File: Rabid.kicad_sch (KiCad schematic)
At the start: 222 parts, among them J1 USB Header, SW1 Esc, SW10 A, SW100 Unused, SW101 Unused, SW102 →, SW11 Z, SW12 LMeta, SW13 F1, SW14 2, SW15 W, SW16 S, SW17 X, SW18 LAlt, SW19 F2, SW20 3, SW21 E, SW22 D, SW23 C, SW24 Unused, SW25 F3, SW26 4, SW27 R, SW28 F, SW29 V, SW3 Tab, SW30 Unused, SW31 F4, SW32 5, SW33 T, SW34 G, SW35 B, SW36 Unused, SW37 F5, SW38 6, SW39 Y, SW4 CapsLk, SW40 H, SW41 N, SW42 Space, SW43 F6, SW44 7, SW45 U, SW46 J, SW47 M, SW48 Unused, SW49 F7, SW5 LShift, SW50 8, SW51 I, SW52 K, SW53 ,, SW54 Unused, SW55 F8, SW56 9, SW57 O, SW58 L, SW59 ., SW6 LCtrl, SW60 Unused, SW61 F9, SW62 0, SW63 P, SW64 ;, SW65 /, SW66 AltGr, SW67 F10, SW68 -, SW69 [, SW7 Unused, SW70 ", SW71 RShift, SW72 RMeta, SW73 F11, SW74 =, SW75 ], SW76 ↲, SW77 Unused, SW78 Fn, SW79 F12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

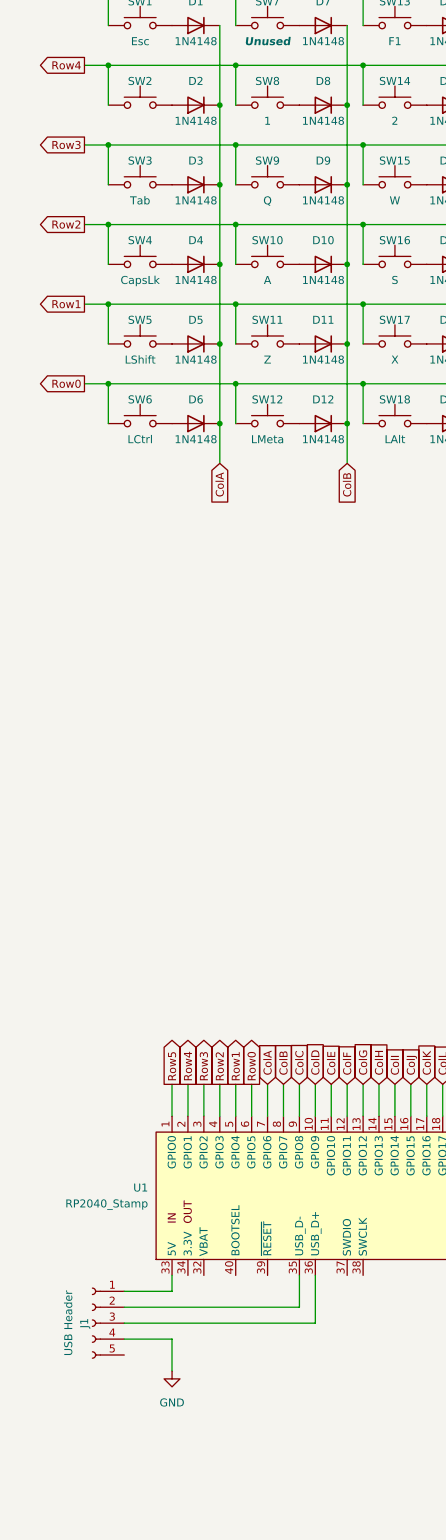
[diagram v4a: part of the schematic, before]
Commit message: Tidy up the USB connector nets.
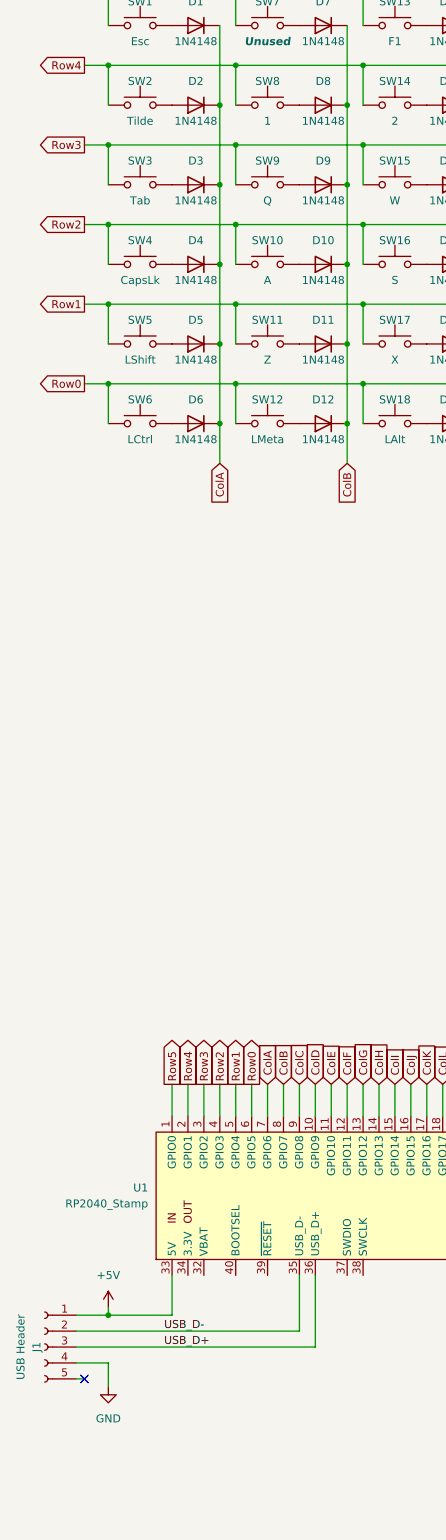
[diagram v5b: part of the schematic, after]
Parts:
- SW2: value ~ -> Tilde
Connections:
- net +5V: now reaches J1.1 (Pin_1), U1.33 (5V)
- net USB_D-: now reaches J1.2 (Pin_2), U1.35 (USB_D-)
- net USB_D+: now reaches J1.3 (Pin_3), U1.36 (USB_D+)
- no-connect marks 0 -> 1
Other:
- moved on the sheet: J1
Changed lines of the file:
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@@
   (junction (at 246.38 60.96) (diameter 0) (color 0 0 0 0)
   )
+  (junction (at 43.18 234.95) (diameter 0) (color 0 0 0 0)
+  )
   (junction (at 167.64 200.66) (diameter 0) (color 0 0 0 0)
   )
@@
   (junction (at 226.06 60.96) (diameter 0) (color 0 0 0 0)
   )
+  (no_connect (at 39.37 245.11))
   (wire (pts (xy 185.42 35.56) (xy 185.42 41.91))
     (stroke (width 0) (type default) (color 0 0 0 0))
@@
     (stroke (width 0) (type default) (color 0 0 0 0))
   )
-  (wire (pts (xy 45.72 236.22) (xy 76.2 236.22))
+  (wire (pts (xy 148.59 204.47) (xy 148.59 200.66))
     (stroke (width 0) (type default) (color 0 0 0 0))
   )
-  (wire (pts (xy 148.59 204.47) (xy 148.59 200.66))
+  (wire (pts (xy 38.1 240.03) (xy 76.2 240.03))
     (stroke (width 0) (type default) (color 0 0 0 0))
   )
@@
     (stroke (width 0) (type default) (color 0 0 0 0))
   )
+  (wire (pts (xy 38.1 242.57) (xy 43.18 242.57))
+    (stroke (width 0) (type default) (color 0 0 0 0))
+  )
   (wire (pts (xy 153.67 191.77) (xy 148.59 191.77))
     (stroke (width 0) (type default) (color 0 0 0 0))
@@
     (stroke (width 0) (type default) (color 0 0 0 0))
   )
-  (wire (pts (xy 45.72 238.76) (xy 53.34 238.76))
-    (stroke (width 0) (type default) (color 0 0 0 0))
-  )
   (wire (pts (xy 347.98 86.36) (xy 368.3 86.36))
     (stroke (width 0) (type default) (color 0 0 0 0))
@@
     (stroke (width 0) (type default) (color 0 0 0 0))
   )
+  (wire (pts (xy 43.18 233.68) (xy 43.18 234.95))
+    (stroke (width 0) (type default) (color 0 0 0 0))
+  )
   (wire (pts (xy 327.66 60.96) (xy 347.98 60.96))
     (stroke (width 0) (type default) (color 0 0 0 0))
@@
     (stroke (width 0) (type default) (color 0 0 0 0))
   )
-  (wire (pts (xy 53.34 228.6) (xy 53.34 231.14))
-    (stroke (width 0) (type default) (color 0 0 0 0))
-  )
   (wire (pts (xy 264.16 29.21) (xy 264.16 41.91))
     (stroke (width 0) (type default) (color 0 0 0 0))
@@
     (stroke (width 0) (type default) (color 0 0 0 0))
   )
+  (wire (pts (xy 38.1 234.95) (xy 43.18 234.95))
+    (stroke (width 0) (type default) (color 0 0 0 0))
+  )
   (wire (pts (xy 78.74 198.12) (xy 78.74 203.2))
     (stroke (width 0) (type default) (color 0 0 0 0))
@@
     (stroke (width 0) (type default) (color 0 0 0 0))
   )
-  (wire (pts (xy 45.72 233.68) (xy 73.66 233.68))
-    (stroke (width 0) (type default) (color 0 0 0 0))
-  )
   (wire (pts (xy 144.78 35.56) (xy 165.1 35.56))
     (stroke (width 0) (type default) (color 0 0 0 0))
@@
     (stroke (width 0) (type default) (color 0 0 0 0))
   )
+  (wire (pts (xy 38.1 245.11) (xy 39.37 245.11))
+    (stroke (width 0) (type default) (color 0 0 0 0))
+  )
   (wire (pts (xy 165.1 73.66) (xy 165.1 80.01))
     (stroke (width 0) (type default) (color 0 0 0 0))
@@
     (stroke (width 0) (type default) (color 0 0 0 0))
   )
+  (wire (pts (xy 43.18 234.95) (xy 53.34 234.95))
+    (stroke (width 0) (type default) (color 0 0 0 0))
+  )
   (wire (pts (xy 182.88 67.31) (xy 182.88 80.01))
     (stroke (width 0) (type default) (color 0 0 0 0))
@@
     (stroke (width 0) (type default) (color 0 0 0 0))
   )
-  (wire (pts (xy 76.2 236.22) (xy 76.2 228.6))
-    (stroke (width 0) (type default) (color 0 0 0 0))
-  )
   (wire (pts (xy 347.98 48.26) (xy 368.3 48.26))
     (stroke (width 0) (type default) (color 0 0 0 0))
@@
     (stroke (width 0) (type default) (color 0 0 0 0))
   )
-  (wire (pts (xy 53.34 238.76) (xy 53.34 243.84))
-    (stroke (width 0) (type default) (color 0 0 0 0))
-  )
   (wire (pts (xy 165.1 86.36) (xy 165.1 92.71))
     (stroke (width 0) (type default) (color 0 0 0 0))
@@
     (stroke (width 0) (type default) (color 0 0 0 0))
   )
+  (wire (pts (xy 43.18 242.57) (xy 43.18 246.38))
+    (stroke (width 0) (type default) (color 0 0 0 0))
+  )
   (wire (pts (xy 161.29 224.79) (xy 167.64 224.79))
     (stroke (width 0) (type default) (color 0 0 0 0))
@@
     (stroke (width 0) (type default) (color 0 0 0 0))
   )
+  (wire (pts (xy 73.66 237.49) (xy 73.66 228.6))
+    (stroke (width 0) (type default) (color 0 0 0 0))
+  )
   (wire (pts (xy 185.42 48.26) (xy 205.74 48.26))
     (stroke (width 0) (type default) (color 0 0 0 0))
@@
     (stroke (width 0) (type default) (color 0 0 0 0))
   )
-  (wire (pts (xy 162.56 41.91) (xy 162.56 54.61))
+  (wire (pts (xy 38.1 237.49) (xy 73.66 237.49))
     (stroke (width 0) (type default) (color 0 0 0 0))
   )
-  (wire (pts (xy 43.18 73.66) (xy 63.5 73.66))
+  (wire (pts (xy 162.56 41.91) (xy 162.56 54.61))
     (stroke (width 0) (type default) (color 0 0 0 0))
   )
-  (wire (pts (xy 73.66 233.68) (xy 73.66 228.6))
+  (wire (pts (xy 43.18 73.66) (xy 63.5 73.66))
     (stroke (width 0) (type default) (color 0 0 0 0))
   )
@@
     (stroke (width 0) (type default) (color 0 0 0 0))
   )
-  (wire (pts (xy 53.34 231.14) (xy 45.72 231.14))
-    (stroke (width 0) (type default) (color 0 0 0 0))
-  )
   (wire (pts (xy 43.18 22.86) (xy 63.5 22.86))
     (stroke (width 0) (type default) (color 0 0 0 0))
@@
     (stroke (width 0) (type default) (color 0 0 0 0))
   )
+  (wire (pts (xy 76.2 240.03) (xy 76.2 228.6))
+    (stroke (width 0) (type default) (color 0 0 0 0))
+  )
   (wire (pts (xy 83.82 48.26) (xy 83.82 54.61))
     (stroke (width 0) (type default) (color 0 0 0 0))
@@
     (stroke (width 0) (type default) (color 0 0 0 0))
   )
+  (wire (pts (xy 53.34 234.95) (xy 53.34 228.6))
+    (stroke (width 0) (type default) (color 0 0 0 0))
+  )
   (wire (pts (xy 83.82 86.36) (xy 104.14 86.36))
     (stroke (width 0) (type default) (color 0 0 0 0))
@@
     (stroke (width 0) (type default) (color 0 0 0 0))
   )
+  (label "USB_D-" (at 52.07 237.49 0)
+    (effects (font (size 1.27 1.27)) (justify left bottom))
+  )
+  (label "USB_D+" (at 52.07 240.03 0)
+    (effects (font (size 1.27 1.27)) (justify left bottom))
+  )
   (global_label "ColE" (shape input) (at 78.74 198.12 90) (fields_autoplaced)
     (effects (font (size 1.27 1.27)) (justify left))
@@
     (pin "2")
   )
+  (symbol (lib_id "power:+5V") (at 43.18 233.68 0) (unit 1)
+    (in_bom yes) (on_board yes) (fields_autoplaced)
+    (property "Reference" "#PWR0101" (id 0) (at 43.18 237.49 0)
+      (effects (font (size 1.27 1.27)) hide)
+    )
+    (property "Value" "+5V" (id 1) (at 43.18 228.6 0))
+    (property "Footprint" "" (id 2) (at 43.18 233.68 0)
+      (effects (font (size 1.27 1.27)) hide)
+    )
+    (property "Datasheet" "" (id 3) (at 43.18 233.68 0)
+      (effects (font (size 1.27 1.27)) hide)
+    )
+    (pin "1")
+  )
   (symbol (lib_id "Switch:SW_Push") (at 48.26 54.61 0) (unit 1)
     (in_bom yes) (on_board yes)
@@
     (pin "2")
   )
-  (symbol (lib_id "power:GND") (at 53.34 243.84 0) (unit 1)
+  (symbol (lib_id "power:GND") (at 43.18 246.38 0) (unit 1)
     (in_bom yes) (on_board yes) (fields_autoplaced)
-    (property "Reference" "#PWR01" (id 0) (at 53.34 250.19 0)
+    (property "Reference" "#PWR01" (id 0) (at 43.18 252.73 0)
       (effects (font (size 1.27 1.27)) hide)
     )
-    (property "Value" "GND" (id 1) (at 53.34 248.92 0))
-    (property "Footprint" "" (id 2) (at 53.34 243.84 0)
+    (property "Value" "GND" (id 1) (at 43.18 251.46 0))
+    (property "Footprint" "" (id 2) (at 43.18 246.38 0)
       (effects (font (size 1.27 1.27)) hide)
     )
-    (property "Datasheet" "" (id 3) (at 53.34 243.84 0)
+    (property "Datasheet" "" (id 3) (at 43.18 246.38 0)
       (effects (font (size 1.27 1.27)) hide)
     )
@@
     (pin "2")
   )
-  (symbol (lib_id "Connector:Conn_01x05_Female") (at 40.64 236.22 0) (mirror y) (unit 1)
+  (symbol (lib_id "Connector:Conn_01x05_Female") (at 33.02 240.03 0) (mirror y) (unit 1)
     (in_bom yes) (on_board yes)
-    (property "Reference" "J1" (id 0) (at 39.37 236.22 90))
-    (property "Value" "USB Header" (id 1) (at 36.83 236.22 90))
-    (property "Footprint" "Connector_JST:JST_PH_S5B-PH-SM4-TB_1x05-1MP_P2.00mm_Horizontal" (id 2) (at 40.64 236.22 0)
+    (property "Reference" "J1" (id 0) (at 31.75 240.03 90))
+    (property "Value" "USB Header" (id 1) (at 29.21 240.03 90))
+    (property "Footprint" "Connector_JST:JST_PH_S5B-PH-SM4-TB_1x05-1MP_P2.00mm_Horizontal" (id 2) (at 33.02 240.03 0)
       (effects (font (size 1.27 1.27)) hide)
     )
-    (property "Datasheet" "~" (id 3) (at 40.64 236.22 0)
+    (property "Datasheet" "~" (id 3) (at 33.02 240.03 0)
       (effects (font (size 1.27 1.27)) hide)
     )
@@
     (in_bom yes) (on_board yes)
     (property "Reference" "SW2" (id 0) (at 48.26 38.1 0))
-    (property "Value" "~" (id 1) (at 48.26 44.45 0))
+    (property "Value" "Tilde" (id 1) (at 48.26 44.45 0))
     (property "Footprint" "Button_Switch_Keyboard:SW_Cherry_MX_1.00u_PCB" (id 2) (at 48.26 36.83 0)
       (effects (font (size 1.27 1.27)) hide)
@@
       (reference "#PWR03") (unit 1) (value "GND") (footprint "")
     )
+    (path "/5f8c35e1-5bf2-4d45-a9cb-08fd83fcfa83"
+      (reference "#PWR0101") (unit 1) (value "+5V") (footprint "")
+    )
     (path "/d4e64c8a-9d33-471d-8397-e938eb6e8f2e"
       (reference "D1") (unit 1) (value "1N4148") (footprint "Diode_THT:D_DO-35_SOD27_P7.62mm_Horizontal")
@@
     )
     (path "/f64a1d2c-ef59-41a1-b199-a5a997fe6eb0"
-      (reference "SW2") (unit 1) (value "~") (footprint "Button_Switch_Keyboard:SW_Cherry_MX_1.00u_PCB")
+      (reference "SW2") (unit 1) (value "Tilde") (footprint "Button_Switch_Keyboard:SW_Cherry_MX_1.00u_PCB")
     )
     (path "/607946a4-b92b-4e67-ac5d-745960c4bf90"

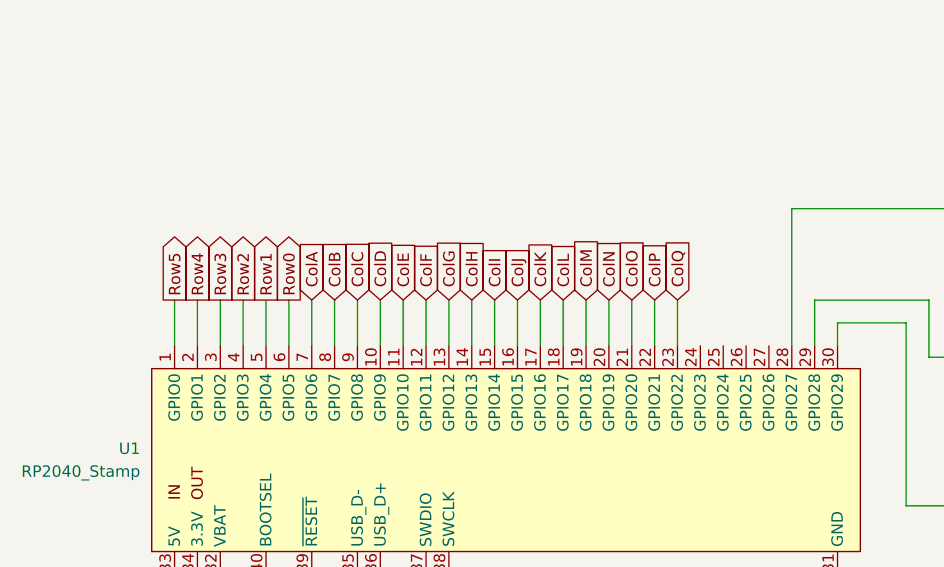
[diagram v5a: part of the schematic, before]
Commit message: Routed arrows keys and rows.
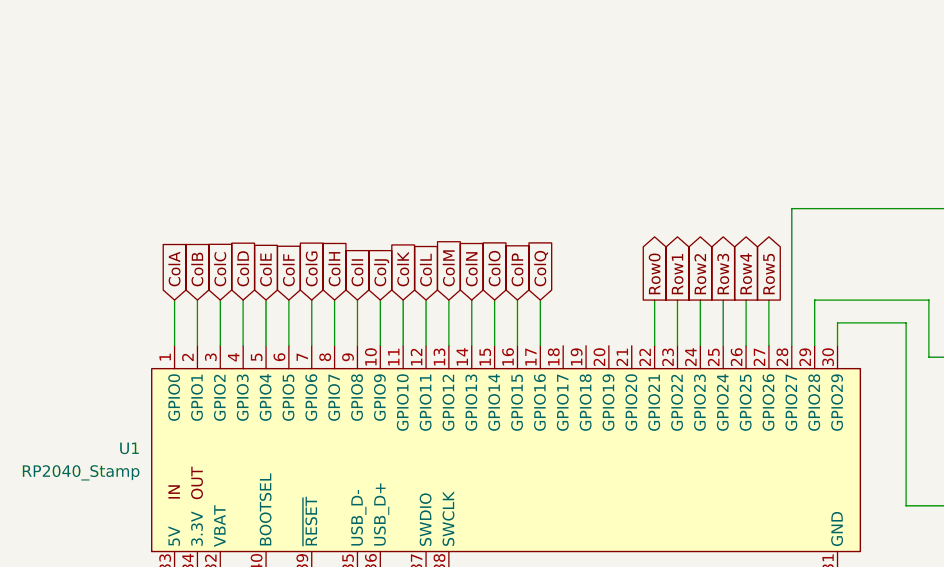
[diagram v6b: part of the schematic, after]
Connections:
- net ColA: now also U1.1 (GPIO0); no longer U1.7 (GPIO6)
- net ColB: now also U1.2 (GPIO1); no longer U1.8 (GPIO7)
- net ColC: now also U1.3 (GPIO2); no longer U1.9 (GPIO8)
- net ColD: now also U1.4 (GPIO3); no longer U1.10 (GPIO9)
- net ColE: now also U1.5 (GPIO4); no longer U1.11 (GPIO10)
- net ColF: now also U1.6 (GPIO5); no longer U1.12 (GPIO11)
- net ColG: now also U1.7 (GPIO6); no longer U1.13 (GPIO12)
- net ColH: now also U1.8 (GPIO7); no longer U1.14 (GPIO13)
- net ColI: now also U1.9 (GPIO8); no longer U1.15 (GPIO14)
- net ColJ: now also U1.10 (GPIO9); no longer U1.16 (GPIO15)
- net ColK: now also U1.11 (GPIO10); no longer U1.17 (GPIO16)
- net ColL: now also U1.12 (GPIO11); no longer U1.18 (GPIO17)
- net ColM: now also U1.13 (GPIO12); no longer U1.19 (GPIO18)
- net ColN: now also U1.14 (GPIO13); no longer U1.20 (GPIO19)
- net ColO: now also U1.15 (GPIO14); no longer U1.21 (GPIO20)
- net ColP: now also U1.16 (GPIO15); no longer U1.22 (GPIO21)
- net ColQ: now also U1.17 (GPIO16); no longer U1.23 (GPIO22)
- net Row0: now also U1.22 (GPIO21); no longer U1.6 (GPIO5)
- net Row1: now also U1.23 (GPIO22); no longer U1.5 (GPIO4)
- net Row2: now also U1.24 (GPIO23); no longer U1.4 (GPIO3)
- net Row3: now also U1.25 (GPIO24); no longer U1.3 (GPIO2)
- net Row4: now also U1.26 (GPIO25); no longer U1.2 (GPIO1)
- net Row5: now also U1.27 (GPIO26); no longer U1.1 (GPIO0)

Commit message: Fixed several DRC errors.
 - Moved silkscreens into component footprints to keep them from overlapping.
 -  Re-routed USB traces as a differential pair.
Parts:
- D1, D10, D102, D11, D12, D13, D14, D15, D16, D17, D18, D19, D2, D20, D21, D22, D23, D25, D26, D27, D28, D29, D3, D31, D32, D33, D34, D35, D37, D38, D39, D4, D40, D41, D42, D43, D44, D45, D46, D47, D49, D5, D50, D51, D52, D53, D55, D56, D57, D58, D59, D6, D61, D62, D63, D64, D65, D66, D67, D68, D69, D70, D71, D72, D73, D74, D75, D76, D78, D79, D8, D80, D81, D84, D85, D86, D87, D9, D90, D91, D92, D93, D95, D96, D97, D98, D99: footprint Diode_THT:D_DO-35_SOD27_P7.62mm_Horizontal -> RabidKeyboard:D_DO-35_SOD27_P7.62mm_Horizontal
- R1, R2, R3: footprint Resistor_THT:R_Axial_DIN0204_L3.6mm_D1.6mm_P7.62mm_Horizontal -> RabidKeyboard:R_Axial_DIN0204_L3.6mm_D1.6mm_P7.62mm_Horizontal
- SW1, SW10, SW102, SW11, SW13, SW14, SW15, SW16, SW17, SW19, SW2, SW20, SW21, SW22, SW23, SW25, SW26, SW27, SW28, SW29, SW31, SW32, SW33, SW34, SW35, SW37, SW38, SW39, SW40, SW41, SW43, SW44, SW45, SW46, SW47, SW49, SW50, SW51, SW52, SW53, SW55, SW56, SW57, SW58, SW59, SW61, SW62, SW63, SW64, SW65, SW67, SW68, SW69, SW70, SW73, SW74, SW75, SW79, SW8, SW85, SW86, SW87, SW9, SW90, SW91, SW92, SW93, SW95, SW96, SW97, SW98, SW99: footprint Button_Switch_Keyboard:SW_Cherry_MX_1.00u_PCB -> RabidKeyboard:SW_Cherry_MX_1.00u_PCB
- SW12, SW18, SW6, SW66, SW72, SW78, SW84: footprint Button_Switch_Keyboard:SW_Cherry_MX_1.25u_PCB -> RabidKeyboard:SW_Cherry_MX_1.25u_PCB
- SW3, SW81: footprint Button_Switch_Keyboard:SW_Cherry_MX_1.50u_PCB -> RabidKeyboard:SW_Cherry_MX_1.50u_PCB
- SW42: footprint Button_Switch_Keyboard:SW_Cherry_MX_6.25u_PCB -> RabidKeyboard:SW_Cherry_MX_6.25u_PCB_MirroredStabs
- SW5, SW76: footprint Button_Switch_Keyboard:SW_Cherry_MX_2.25u_PCB -> RabidKeyboard:SW_Cherry_MX_2.25u_PCB
- SW71: footprint Button_Switch_Keyboard:SW_Cherry_MX_2.75u_PCB -> RabidKeyboard:SW_Cherry_MX_2.75u_PCB
- SW80: footprint Button_Switch_Keyboard:SW_Cherry_MX_2.00u_PCB -> RabidKeyboard:SW_Cherry_MX_2.00u_PCB
